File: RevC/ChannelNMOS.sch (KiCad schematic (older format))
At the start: 2 parts, among them U2 RAx4_4 1K

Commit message: updates
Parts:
- QLOAD1: LcscNo (none) -> C20526
- U2: Type (none) -> C396839
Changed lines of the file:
@@
 $Descr A4 11693 8268
 encoding utf-8
-Sheet 26 29
+Sheet 20 29
 Title ""
 Date ""
@@
 AR Path="/5E2651B2/5EAB52D0" Ref="U16"  Part="1"
 AR Path="/5E29F140/5EAB52D0" Ref="U18"  Part="1"
-F 0 "U16" V 6554 4063 50  0000 L CNN
+F 0 "U2" V 6554 4063 50  0000 L CNN
 F 1 "RAx4_4 1K" V 6645 4063 50  0000 L CNN
 F 2 "Resistor_SMD:R_Array_Convex_4x0603" H 6600 3875 50  0001 C CNN
-F 3 "" H 6600 3975 50  0001 C CNN
+F 3 "https://datasheet.lcsc.com/szlcsc/1912111437_HX-hengjiaxing-HX2301A_C296298.pdf" H 6600 3975 50  0001 C CNN
+F 4 "C396839" V 6600 3975 50  0001 C CNN "Type"
 	1    6600 3975
 	0    1    1    0
@@
 AR Path="/5E2651B2/5E01FEAF" Ref="QLOAD8"  Part="1"
 AR Path="/5E29F140/5E01FEAF" Ref="QLOAD9"  Part="1"
-F 0 "QLOAD8" H 6691 4921 50  0000 L CNN
+F 0 "QLOAD1" H 6691 4921 50  0000 L CNN
 F 1 "MMBT3904" H 6691 4830 50  0000 L CNN
 F 2 "Package_TO_SOT_SMD:SOT-23" H 6700 4800 50  0001 L CIN
-F 3 "https://www.fairchildsemi.com/datasheets/2N/2N3904.pdf" H 6500 4875 50  0001 L CNN
+F 3 "https://datasheet.lcsc.com/szlcsc/1810202112_Guangdong-Hottech-MMBT3904_C181119.pdf" H 6500 4875 50  0001 L CNN
+F 4 "C20526" H 6500 4875 50  0001 C CNN "LcscNo"
 	1    6500 4875
 	1    0    0    -1

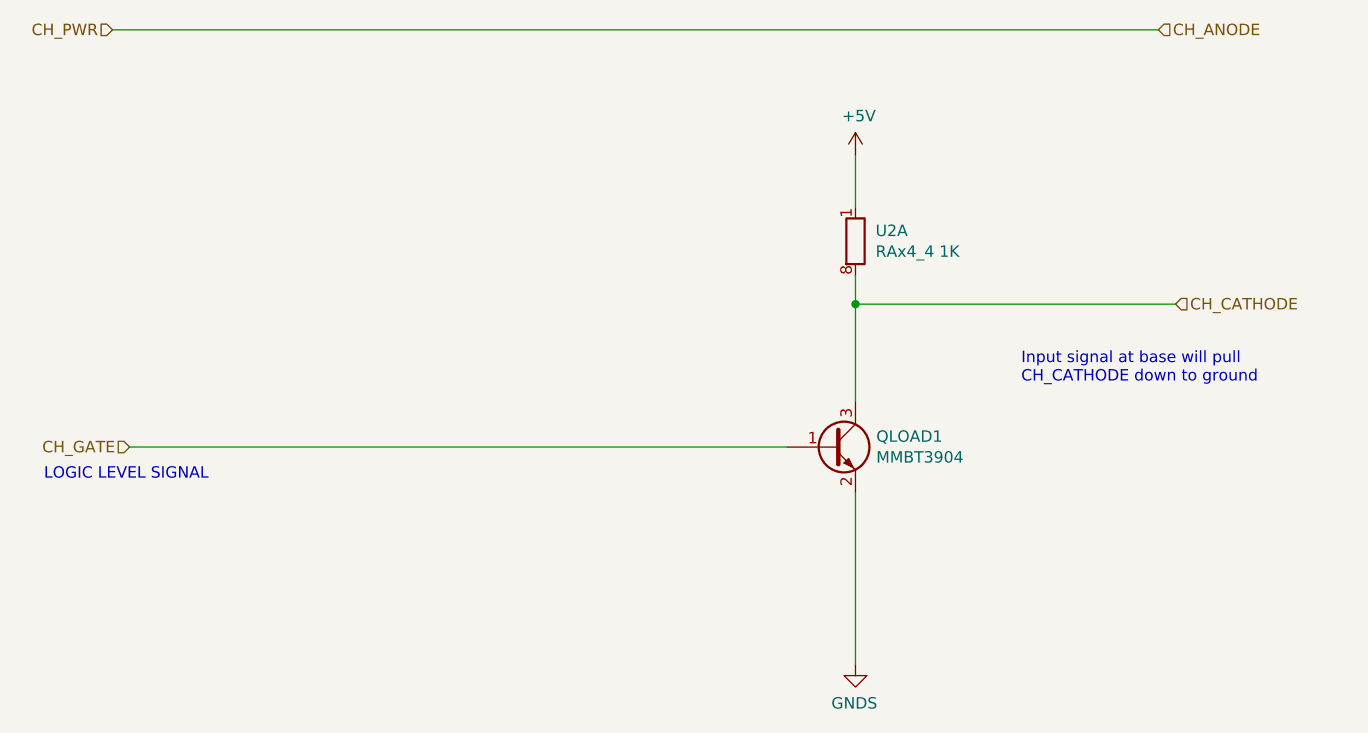
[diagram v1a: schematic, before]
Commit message: Replaced 6N135 SMDIP8 with H11L1 SMDIP6
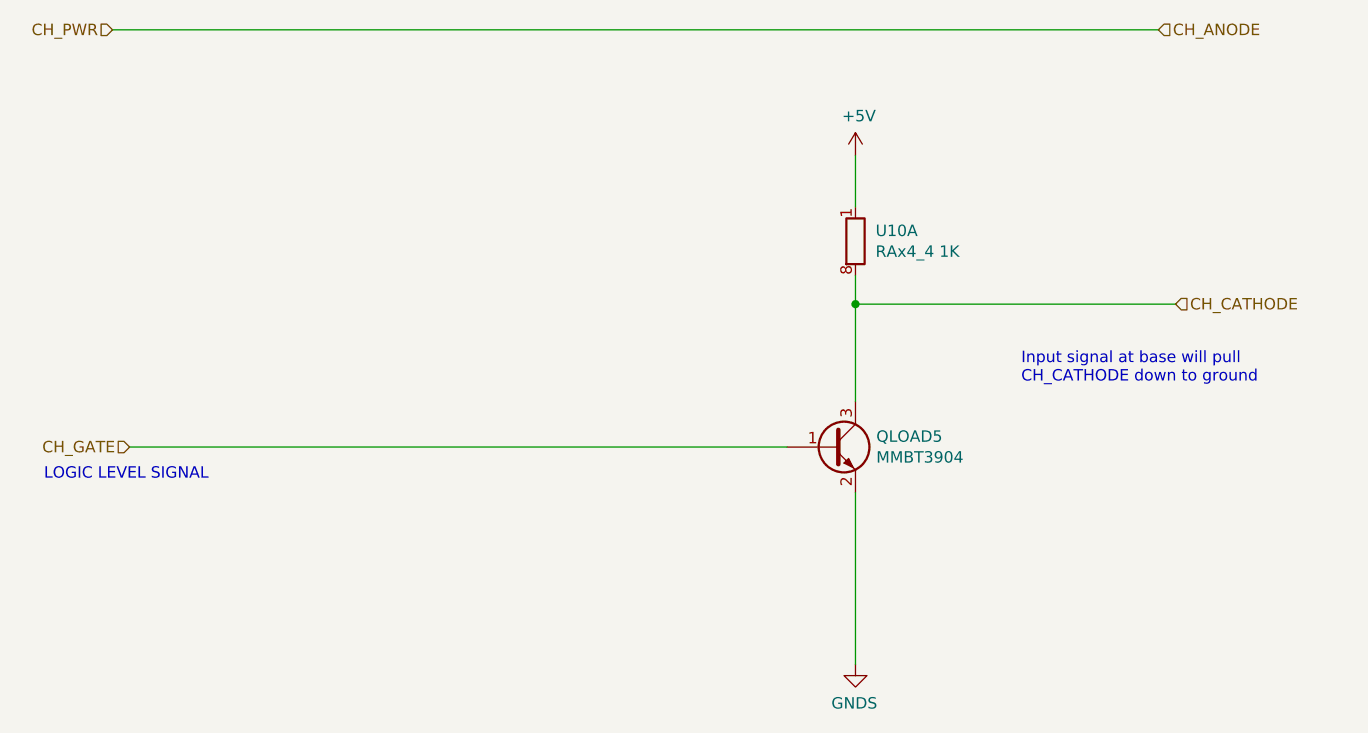
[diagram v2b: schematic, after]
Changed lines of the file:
@@
 AR Path="/5E2651B2/5EAB52D0" Ref="U16"  Part="1"
 AR Path="/5E29F140/5EAB52D0" Ref="U18"  Part="1"
-F 0 "U2" V 6554 4063 50  0000 L CNN
+F 0 "U10" V 6554 4063 50  0000 L CNN
 F 1 "RAx4_4 1K" V 6645 4063 50  0000 L CNN
 F 2 "Resistor_SMD:R_Array_Convex_4x0603" H 6600 3875 50  0001 C CNN
@@
 AR Path="/5E2651B2/5E01FEAF" Ref="QLOAD8"  Part="1"
 AR Path="/5E29F140/5E01FEAF" Ref="QLOAD9"  Part="1"
-F 0 "QLOAD1" H 6691 4921 50  0000 L CNN
+F 0 "QLOAD5" H 6691 4921 50  0000 L CNN
 F 1 "MMBT3904" H 6691 4830 50  0000 L CNN
 F 2 "Package_TO_SOT_SMD:SOT-23" H 6700 4800 50  0001 L CIN
